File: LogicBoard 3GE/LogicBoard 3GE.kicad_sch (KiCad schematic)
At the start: 170 parts, among them IC103 LM386-3, IC201 27C512PLCC, IC202 74LS00, IC203 74LS32, IC204 CY62256-70PC, IC206 68A09, IC207 6522, IC208 AY3-8912, IC301 MC1408, IC302 CD4052B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

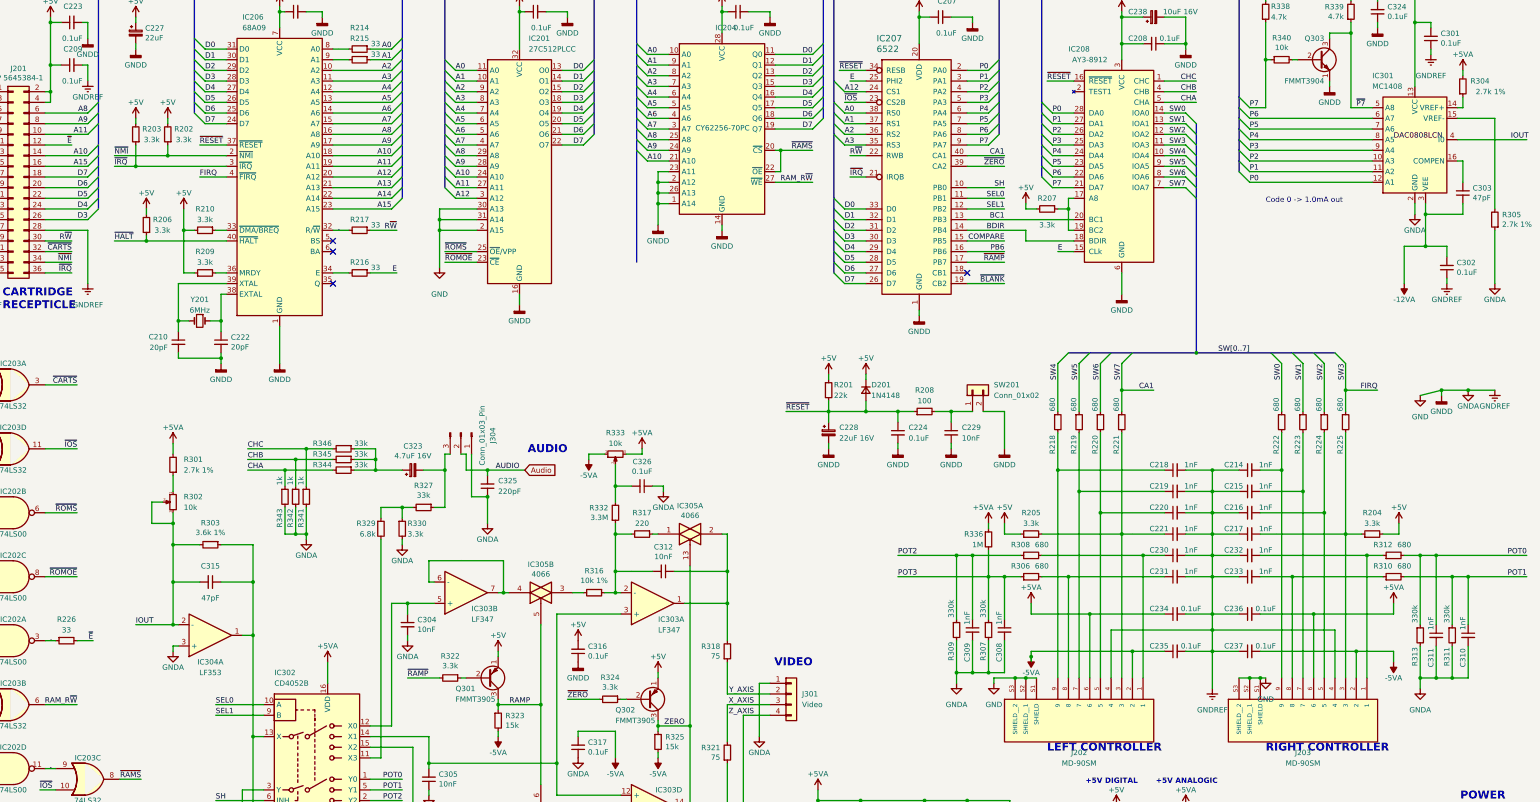
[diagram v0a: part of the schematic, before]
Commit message: changed packages and symbols to fit Mouser BOM
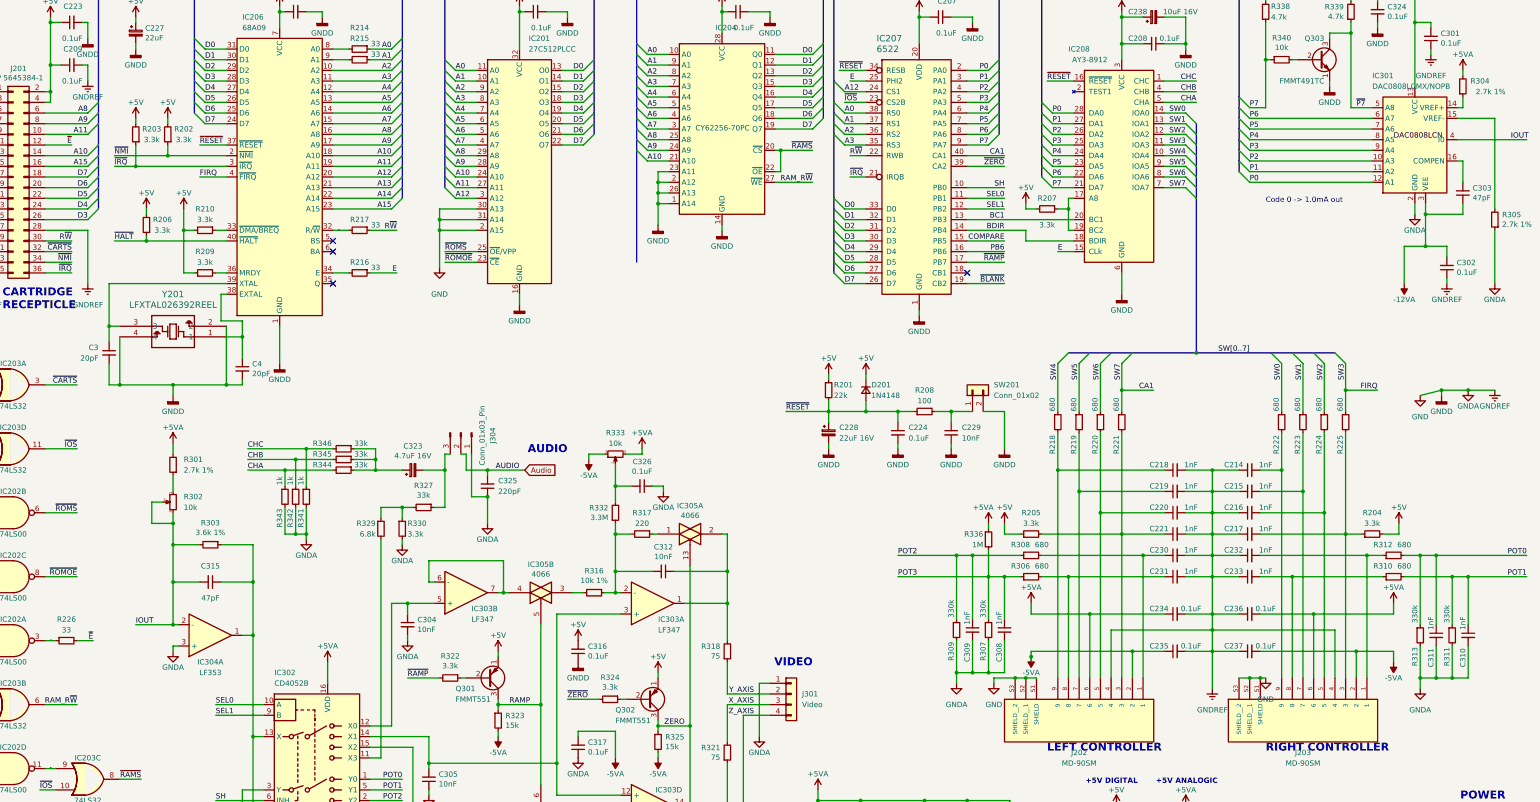
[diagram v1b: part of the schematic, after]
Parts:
- removed C210, C222: 20pF, Capacitor_SMD:C_0805_2012Metric, symbol Device:C_Small
- removed Y201: 6MHz, Crystal:Crystal_SMD_7050-2Pin_7.0x5.0mm, symbol Device:Crystal_Small
- added C3, C4: 20pF, Capacitor_SMD:C_0805_2012Metric, symbol Device:C_Small
- added Y201: LFXTAL026392REEL, 12SMX-B_7x5-SMD_IQD, symbol Crystal:LFXTAL026392REEL
- C113: footprint Capacitor_Tantalum_SMD:CP_EIA-7260-15_AVX-R_Pad2.68x6.30mm_HandSolder -> Capacitor_Tantalum_SMD:CP_EIA-3216-18_Kemet-A; Mouser (none) -> https://www.mouser.es/ProductDetail/KYOCERA-AVX/F931C106MAA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
- C114: footprint Capacitor_Tantalum_SMD:CP_EIA-7260-15_AVX-R_Pad2.68x6.30mm_HandSolder -> Capacitor_Tantalum_SMD:CP_EIA-3216-18_Kemet-A
- C211: footprint Capacitor_Tantalum_SMD:CP_EIA-3528-15_AVX-H -> Capacitor_Tantalum_SMD:CP_EIA-7343-15_Kemet-W; Mouser (none) -> https://www.mouser.es/ProductDetail/KEMET/T491X227M016AT?qs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
- C212, C213: footprint Capacitor_Tantalum_SMD:CP_EIA-3528-15_AVX-H -> Capacitor_Tantalum_SMD:CP_EIA-7343-43_Kemet-X
- C227, C228: footprint Capacitor_Tantalum_SMD:CP_EIA-3528-15_AVX-H -> Capacitor_Tantalum_SMD:CP_EIA-7343-31_Kemet-D
- C238: footprint Capacitor_Tantalum_SMD:CP_EIA-3528-15_AVX-H -> Capacitor_Tantalum_SMD:CP_EIA-7343-31_Kemet-D; Mouser (none) -> https://www.mouser.es/ProductDetail/Vishay-Sprague/293D226X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
- C323: footprint Capacitor_Tantalum_SMD:CP_EIA-3528-15_AVX-H -> Capacitor_Tantalum_SMD:CP_EIA-3528-21_Kemet-B; Mouser 647-UkT1E4R7MDD1TD -> 74-293D226X9035D2TE3
- IC301: value MC1408 -> DAC0808LCMX/NOPB; Mouser 926-DAC0808LCN/NOPB -> DAC0808LCMX/NOPB
- Q301, Q302: value FMMT3905 -> FMMT551; Mouser (none) -> 522-FMMT551TA
- Q303: value FMMT3904 -> FMMT491TC; Mouser 512-2N3904TA -> 522-FMMT491TC
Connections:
- net EXTAL: now also C4.1, Y201.1
- net GND: now also C3.2, C4.2, Y201.2, Y201.4
- net XTAL: now also C3.1, Y201.3
